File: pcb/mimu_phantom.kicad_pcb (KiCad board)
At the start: 2 copper layers, 50 x 27 mm, 36 parts, among them J1 OPT, Q1 BSS84, SW1 SW_Push, SW2 In case mosfet does not work 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, U1 PC817, U2 ATTINY88AU, U3 MCP16331CH, U4 AD5258

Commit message: Initial playarounds for rheostat mode
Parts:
- removed R5: 12R, Resistor_SMD:R_1206_3216Metric_Pad1.30x1.75mm_HandSolder
- added C4: 0.1 nF, Resistor_SMD:R_1206_3216Metric_Pad1.30x1.75mm_HandSolder, F.Cu at (121.2, 78.5)
- R6: value 68R -> 300R
- U1: value PC817 -> NSL-32SR3
- U4: value AD5258 -> AD5258 - 1k
- moved SW2 7.16 mm to (131.0, 78.8)
- moved R6 3.35 mm to (124.8, 78.5)
- moved TP1 2.74 mm to (124.0, 74.0)
- moved U4 0.90 mm to (128.2, 78.0)
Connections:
- C_B1 pad 2: Net-(C_B1-Pad2) -> Net-(D1-K)
- L1 pad 2: Net-(C_B1-Pad2) -> Net-(D1-K)
- Q1 pad 3: Net-(SW2-Pad2) -> Net-(Q1-D)
- R6 pad 1: Net-(SW2-Pad2) -> Net-(U4-W)
- SW2 pad 2: Net-(SW2-Pad2) -> Net-(Q1-D)
- U3 pad 6: Net-(C_B1-Pad2) -> Net-(D1-K)
- U4 pad 1: Net-(R5-Pad1) -> Net-(U4-W)
- U4 pad 10: VCC -> Net-(Q1-D)
- U4 pad 9: XLR_GND -> unconnected-(U4-B-Pad9)
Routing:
- net Net-(C_B1-Pad2): track 26.2 -> 0.00 mm
- net Net-(SW2-Pad2): track 23.3 -> 0.00 mm, vias 3 -> 0
- net Net-(D1-K): track 0.00 -> 17.4 mm
- net Net-(Q1-D): track 0.00 -> 9.45 mm
- net XLR_GND: track 111.4 -> 106.5 mm
- net Net-(R5-Pad1): track 4.34 -> 0.00 mm, vias 2 -> 0
- net Net-(U4-W): track 0.00 -> 4.29 mm
- net Net-(C4-Pad1): track 17.6 -> 21.3 mm, vias 0 -> 2
- net +BATT: track 54.0 -> 50.9 mm
- net VCC: track 119.1 -> 118.0 mm
- net SCL: track 18.2 -> 19.0 mm

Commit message: Small cleanups
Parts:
- moved C_pre1 2.02 mm to (115.6, 78.5)
- moved C_pre2 2.02 mm to (118.3, 78.5)
- moved TP1 1.00 mm to (123.0, 74.2)
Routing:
- net +BATT: track 50.9 -> 54.6 mm
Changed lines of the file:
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@@
 	(footprint "Measurement_Points:Measurement_Point_Round-SMD-Pad_Small"
 		(layer "F.Cu")
-		(at 123.975 74.025)
+		(at 123 74.25)
 		(descr "Mesurement Point, Round, SMD Pad, DM 1.5mm,")
 		(tags "Mesurement Point Round SMD Pad 1.5mm")
@@
 	(footprint "Capacitor_SMD:C_1206_3216Metric_Pad1.33x1.80mm_HandSolder"
 		(layer "F.Cu")
-		(at 115.9 76.5 -90)
+		(at 115.6 78.5 -90)
 		(descr "Capacitor SMD 1206 (3216 Metric), square (rectangular) end terminal, IPC_7351 nominal with elongated pad for handsoldering. (Body size source: IPC-SM-782 page 76, https://www.pcb-3d.com/wordpress/wp-content/uploads/ipc-sm-782a_amendment_1_and_2.pdf), generated with kicad-footprint-generator")
 		(tags "capacitor handsolder")
@@
 		(tags "resistor handsolder")
 		(property "Reference" "R6"
-			(at -3.1 0.1 180)
+			(at -3.1 -0.5 180)
 			(layer "F.SilkS")
 			(effects
@@
 		(tags "resistor handsolder")
 		(property "Reference" "C4"
-			(at 0 -1.82 270)
+			(at 3.25 0 0)
 			(layer "F.SilkS")
 			(effects
@@
 	(footprint "Capacitor_SMD:C_1206_3216Metric_Pad1.33x1.80mm_HandSolder"
 		(layer "F.Cu")
-		(at 118.6 76.5 -90)
+		(at 118.3 78.5 -90)
 		(descr "Capacitor SMD 1206 (3216 Metric), square (rectangular) end terminal, IPC_7351 nominal with elongated pad for handsoldering. (Body size source: IPC-SM-782 page 76, https://www.pcb-3d.com/wordpress/wp-content/uploads/ipc-sm-782a_amendment_1_and_2.pdf), generated with kicad-footprint-generator")
 		(tags "capacitor handsolder")
@@
 	)
 	(segment
-		(start 102.6875 75.0125)
-		(end 101.45 76.25)
+		(start 123 81)
+		(end 123 76)
 		(width 0.75)
 		(layer "F.Cu")
@@
 	)
 	(segment
-		(start 123 81)
-		(end 123 75.052632)
+		(start 102.6875 75.0125)
+		(end 101.45 76.25)
 		(width 0.75)
 		(layer "F.Cu")
@@
 	)
 	(segment
+		(start 123 76)
+		(end 122.0125 75.0125)
+		(width 0.75)
+		(layer "F.Cu")
+		(net 11)
+	)
+	(segment
+		(start 124.25 82.9)
+		(end 123 81)
+		(width 0.75)
+		(layer "F.Cu")
+		(net 11)
+	)
+	(segment
 		(start 124.25 85.2)
 		(end 124 85.45)
@@
 	)
 	(segment
-		(start 123.025 74.975)
-		(end 123.975 74.025)
+		(start 115.6 76.1125)
+		(end 115.6 76.9375)
+		(width 0.75)
+		(layer "F.Cu")
+		(net 11)
+	)
+	(segment
+		(start 122.05 75.2)
+		(end 123 74.25)
 		(width 0.25)
 		(layer "F.Cu")
@@
 	)
 	(segment
-		(start 115.8125 75.025)
-		(end 115.9 74.9375)
-		(width 1)
+		(start 118.3 75.9625)
+		(end 118.3 76.9375)
+		(width 0.75)
 		(layer "F.Cu")
 		(net 11)
@@
 	)
 	(segment
-		(start 122.5 74.6)
-		(end 115.8 74.6)
+		(start 122.0125 75.0125)
+		(end 119.25 75.0125)
 		(width 0.75)
 		(layer "F.Cu")
@@
 	)
 	(segment
-		(start 115.825 75.0125)
-		(end 115.9 74.9375)
+		(start 119.25 75.0125)
+		(end 118.3 75.9625)
 		(width 0.75)
 		(layer "F.Cu")
@@
 	)
 	(segment
-		(start 123 81)
-		(end 124.25 82.9)
+		(start 114.5 75.0125)
+		(end 115.6 76.1125)
 		(width 0.75)
 		(layer "F.Cu")
@@
 	)
 	(segment
-		(start 122.973684 75.026316)
-		(end 122.5 74.6)
+		(start 116 75.0125)
+		(end 114.5 75.0125)
 		(width 0.75)
 		(layer "F.Cu")
@@
 	)
 	(segment
-		(start 111.35 83.284998)
-		(end 111.35 84)
-		(width 0.5)
+		(start 119.25 75.0125)
+		(end 116 75.0125)
+		(width 0.75)
 		(layer "F.Cu")
 		(net 11)
 	)
 	(segment
-		(start 123 75.052632)
-		(end 122.973684 75.026316)
-		(width 0.75)
+		(start 111.35 83.284998)
+		(end 111.35 84)
+		(width 0.5)
 		(layer "F.Cu")
 		(net 11)
 	)
 	(segment
-		(start 106.6 75.0125)
-		(end 115.825 75.0125)
+		(start 114.5 75.0125)
+		(end 106.6 75.0125)
 		(width 0.75)
 		(layer "F.Cu")
@@
 	)
 	(via
-		(at 119.3 78.5)
+		(at 119 80.5)
 		(size 0.8)
 		(drill 0.4)
@@
 	)
 	(via
-		(at 116.5 78.5)
+		(at 116.2 80.5)
 		(size 0.8)
 		(drill 0.4)
@@
 	)
 	(via
-		(at 117.9 78.5)
+		(at 117.6 80.5)
 		(size 0.8)
 		(drill 0.4)
@@
 	)
 	(via
-		(at 115.1 78.5)
+		(at 114.8 80.5)
 		(size 0.8)
 		(drill 0.4)

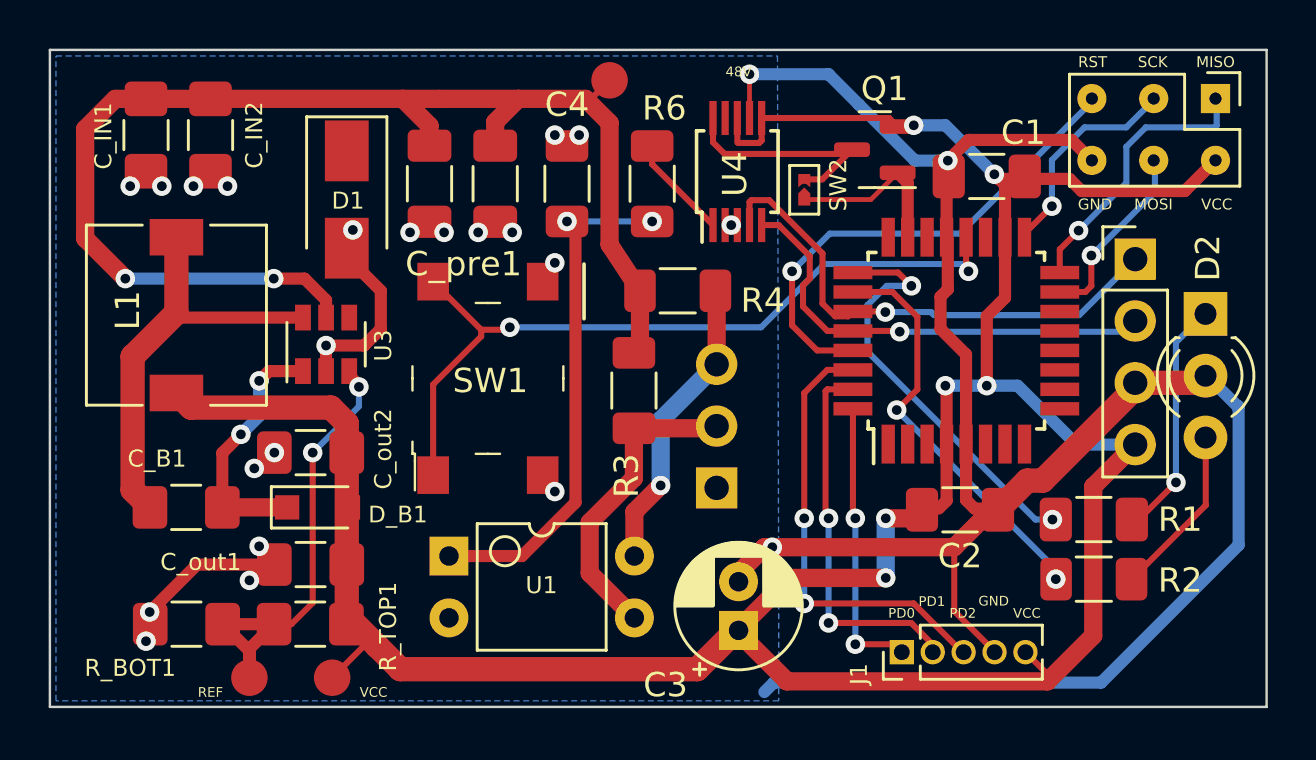
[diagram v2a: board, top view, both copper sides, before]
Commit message: Some goof-arounds, but real prototype still produces wobbles with sensor current draw
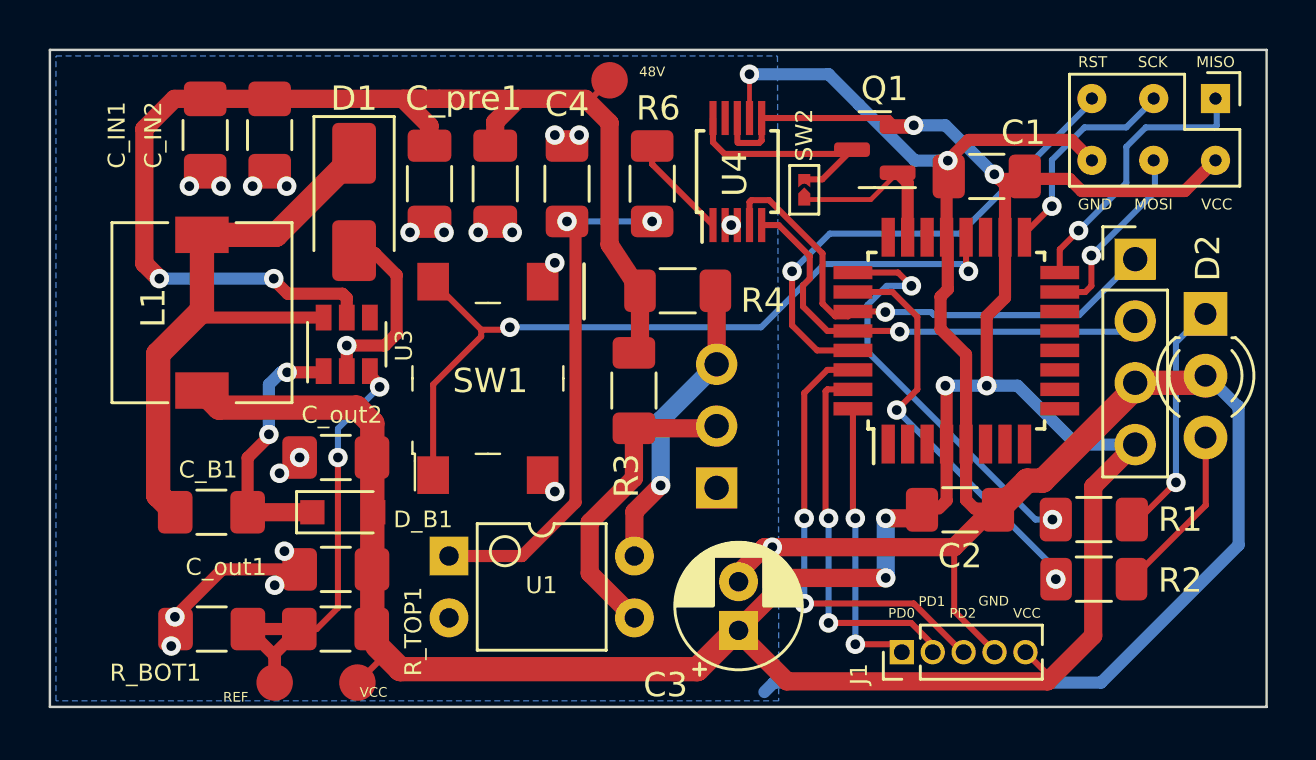
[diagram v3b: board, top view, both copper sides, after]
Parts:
- C_IN1, C_IN2: value 10uF @ 24v -> 10uF @ 48v
- C_pre1: value 3-4uF @24V -> 3-4uF @48V
- C_pre2: value 3-4uF @24V -> 3-4uF @48v
- moved C_IN2 2.43 mm to (109.0, 76.5)
- moved C_IN1 2.43 mm to (106.4, 76.5)
- moved C_B1 1.06 mm to (106.6, 92.0)
- moved R_BOT1 1.06 mm to (106.7, 96.8)
- moved TP3 1.06 mm to (112.6, 99.0)
- moved C_out2 1.06 mm to (111.8, 89.8)
- moved D_B1 1.06 mm to (112.0, 92.0)
- moved R_TOP1 1.06 mm to (111.7, 96.8)
- moved TP4 1.06 mm to (109.2, 99.0)
- moved C_out1 1.06 mm to (111.8, 94.3)
- moved L1 1.05 mm to (106.2, 83.8)
- moved U3 0.85 mm to (112.2, 85.1)
- moved D1 0.32 mm to (112.5, 79.2)
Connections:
- D1 pad 1: Net-(C_B1-Pad2) -> Net-(D1-K)
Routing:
- net Net-(D1-K): track 17.4 -> 25.3 mm
- net VCC: track 118.0 -> 115.7 mm
- net +BATT: track 54.6 -> 53.7 mm
- net XLR_GND: track 106.5 -> 106.9 mm, vias 24 -> 23
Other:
- board text added: "MIMU Phantom v4 PP 04.24"
- board text removed: "MIMU Phantom v3 PP 12.22"
